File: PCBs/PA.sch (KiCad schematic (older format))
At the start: 16 parts, among them K1 TIANBO-HJR-4102-L, Q4 BS170, Q6 BS170, Q8 BS170, Q9 BC849, U1 74AC14

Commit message: ADX988 CAT: add FE, FI commands
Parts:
- C27: footprint Capacitors_THT:C_Disc_D4.7mm_W2.5mm_P5.00mm -> LCSDR:C_1206_0603
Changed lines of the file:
@@
 $Descr A4 11693 8268
 encoding utf-8
-Sheet 6 9
+Sheet 6 8
 Title ""
 Date ""
@@
 Connection ~ 6150 2800
 $Comp
-L GND #PWR060
+L GND #PWR83
 U 1 1 63065D00
 P 6700 3050
-F 0 "#PWR060" H 6700 2800 50  0001 C CNN
+F 0 "#PWR83" H 6700 2800 50  0001 C CNN
 F 1 "GND" H 6700 2900 50  0001 C CNN
 F 2 "" H 6700 3050 50  0001 C CNN
@@
 	6700 3050 6700 3000
 $Comp
-L GND #PWR061
+L GND #PWR85
 U 1 1 63065D9F
 P 7350 3750
-F 0 "#PWR061" H 7350 3500 50  0001 C CNN
+F 0 "#PWR85" H 7350 3500 50  0001 C CNN
 F 1 "GND" H 7350 3600 50  0001 C CNN
 F 2 "" H 7350 3750 50  0001 C CNN
@@
 	7350 3750 7350 3700
 $Comp
-L GND #PWR062
+L GND #PWR81
 U 1 1 63065E88
 P 4850 2600
-F 0 "#PWR062" H 4850 2350 50  0001 C CNN
+F 0 "#PWR81" H 4850 2350 50  0001 C CNN
 F 1 "GND" H 4850 2450 50  0001 C CNN
 F 2 "" H 4850 2600 50  0001 C CNN
@@
 Connection ~ 2100 5500
 $Comp
-L GND #PWR063
+L GND #PWR75
 U 1 1 630683A0
 P 2850 5700
-F 0 "#PWR063" H 2850 5450 50  0001 C CNN
+F 0 "#PWR75" H 2850 5450 50  0001 C CNN
 F 1 "GND" H 2850 5550 50  0001 C CNN
 F 2 "" H 2850 5700 50  0001 C CNN
@@
 $EndComp
 $Comp
-L +5V #PWR064
+L +5V #PWR74
 U 1 1 6306844B
 P 2850 5300
-F 0 "#PWR064" H 2850 5150 50  0001 C CNN
+F 0 "#PWR74" H 2850 5150 50  0001 C CNN
 F 1 "+5V" H 2850 5440 50  0000 C CNN
 F 2 "" H 2850 5300 50  0001 C CNN
@@
 $EndComp
 $Comp
-L GND #PWR065
+L GND #PWR73
 U 1 1 6306851D
 P 2850 4550
-F 0 "#PWR065" H 2850 4300 50  0001 C CNN
+F 0 "#PWR73" H 2850 4300 50  0001 C CNN
 F 1 "GND" H 2850 4400 50  0001 C CNN
 F 2 "" H 2850 4550 50  0001 C CNN
@@
 	2850 4550 2850 4450
 $Comp
-L +5V #PWR066
+L +5V #PWR72
 U 1 1 63068670
 P 2850 4150
-F 0 "#PWR066" H 2850 4000 50  0001 C CNN
+F 0 "#PWR72" H 2850 4000 50  0001 C CNN
 F 1 "+5V" H 2850 4290 50  0000 C CNN
 F 2 "" H 2850 4150 50  0001 C CNN
@@
 	2850 4150 2850 4250
 $Comp
-L GND #PWR067
+L GND #PWR80
 U 1 1 63068793
 P 4350 2600
-F 0 "#PWR067" H 4350 2350 50  0001 C CNN
+F 0 "#PWR80" H 4350 2350 50  0001 C CNN
 F 1 "GND" H 4350 2450 50  0001 C CNN
 F 2 "" H 4350 2600 50  0001 C CNN
@@
 CLK0
 $Comp
-L GND #PWR068
+L GND #PWR77
 U 1 1 63068BDA
 P 2850 6850
-F 0 "#PWR068" H 2850 6600 50  0001 C CNN
+F 0 "#PWR77" H 2850 6600 50  0001 C CNN
 F 1 "GND" H 2850 6700 50  0001 C CNN
 F 2 "" H 2850 6850 50  0001 C CNN
@@
 	2850 6850 2850 6750
 $Comp
-L +5V #PWR069
+L +5V #PWR76
 U 1 1 63068C63
 P 2850 6450
-F 0 "#PWR069" H 2850 6300 50  0001 C CNN
+F 0 "#PWR76" H 2850 6300 50  0001 C CNN
 F 1 "+5V" H 2850 6590 50  0000 C CNN
 F 2 "" H 2850 6450 50  0001 C CNN
@@
 	2850 6450 2850 6550
 $Comp
-L GND #PWR070
+L GND #PWR71
 U 1 1 63068D65
 P 2850 3500
-F 0 "#PWR070" H 2850 3250 50  0001 C CNN
+F 0 "#PWR71" H 2850 3250 50  0001 C CNN
 F 1 "GND" H 2850 3350 50  0001 C CNN
 F 2 "" H 2850 3500 50  0001 C CNN
@@
 	2850 3200 2850 3100
 $Comp
-L +5V #PWR071
+L +5V #PWR70
 U 1 1 63068E93
 P 2850 3100
-F 0 "#PWR071" H 2850 2950 50  0001 C CNN
+F 0 "#PWR70" H 2850 2950 50  0001 C CNN
 F 1 "+5V" H 2850 3240 50  0000 C CNN
 F 2 "" H 2850 3100 50  0001 C CNN
@@
 $EndComp
 $Comp
-L GND #PWR072
+L GND #PWR69
 U 1 1 63068F01
 P 2850 2500
-F 0 "#PWR072" H 2850 2250 50  0001 C CNN
+F 0 "#PWR69" H 2850 2250 50  0001 C CNN
 F 1 "GND" H 2850 2350 50  0001 C CNN
 F 2 "" H 2850 2500 50  0001 C CNN
@@
 	2850 2500 2850 2400
 $Comp
-L +5V #PWR073
+L +5V #PWR68
 U 1 1 63069009
 P 2850 2100
-F 0 "#PWR073" H 2850 1950 50  0001 C CNN
+F 0 "#PWR68" H 2850 1950 50  0001 C CNN
 F 1 "+5V" H 2850 2240 50  0000 C CNN
 F 2 "" H 2850 2100 50  0001 C CNN
@@
 	2850 2100 2850 2200
 $Comp
-L +5V #PWR074
+L +5V #PWR66
 U 1 1 63069127
 P 2850 1000
-F 0 "#PWR074" H 2850 850 50  0001 C CNN
+F 0 "#PWR66" H 2850 850 50  0001 C CNN
 F 1 "+5V" H 2850 1140 50  0000 C CNN
 F 2 "" H 2850 1000 50  0001 C CNN
@@
 $EndComp
 $Comp
-L GND #PWR075
+L GND #PWR67
 U 1 1 6306916E
 P 2850 1400
-F 0 "#PWR075" H 2850 1150 50  0001 C CNN
+F 0 "#PWR67" H 2850 1150 50  0001 C CNN
 F 1 "GND" H 2850 1250 50  0001 C CNN
 F 2 "" H 2850 1400 50  0001 C CNN
@@
 $EndComp
 $Comp
-L GND #PWR076
+L GND #PWR79
 U 1 1 6306940A
 P 4150 1400
-F 0 "#PWR076" H 4150 1150 50  0001 C CNN
+F 0 "#PWR79" H 4150 1150 50  0001 C CNN
 F 1 "GND" H 4150 1250 50  0001 C CNN
 F 2 "" H 4150 1400 50  0001 C CNN
@@
 	4150 1350 4150 1400
 $Comp
-L +5V #PWR077
+L +5V #PWR78
 U 1 1 630694A1
 P 4150 1100
-F 0 "#PWR077" H 4150 950 50  0001 C CNN
+F 0 "#PWR78" H 4150 950 50  0001 C CNN
 F 1 "+5V" H 4150 1240 50  0000 C CNN
 F 2 "" H 4150 1100 50  0001 C CNN
@@
 F 0 "C27" H 8100 3600 50  0000 L CNN
 F 1 "100pF" H 8100 3500 50  0000 L CNN
-F 2 "Capacitors_THT:C_Disc_D4.7mm_W2.5mm_P5.00mm" H 8000 3500 50  0001 C CNN
+F 2 "LCSDR:C_1206_0603" H 8000 3500 50  0001 C CNN
 F 3 "" H 8000 3500 50  0001 C CNN
 	1    8000 3500
@@
 $EndComp
 $Comp
-L GND #PWR078
+L GND #PWR86
 U 1 1 6306993E
 P 8000 3700
-F 0 "#PWR078" H 8000 3450 50  0001 C CNN
+F 0 "#PWR86" H 8000 3450 50  0001 C CNN
 F 1 "GND" H 8000 3550 50  0001 C CNN
 F 2 "" H 8000 3700 50  0001 C CNN
@@
 $EndComp
 $Comp
-L GND #PWR079
+L GND #PWR89
 U 1 1 6306C621
 P 9750 5200
-F 0 "#PWR079" H 9750 4950 50  0001 C CNN
+F 0 "#PWR89" H 9750 4950 50  0001 C CNN
 F 1 "GND" H 9750 5050 50  0001 C CNN
 F 2 "" H 9750 5200 50  0001 C CNN
@@
 $EndComp
 $Comp
-L +12V #PWR080
+L +12V #PWR87
 U 1 1 6306CB0A
 P 8900 3600
-F 0 "#PWR080" H 8900 3450 50  0001 C CNN
+F 0 "#PWR87" H 8900 3450 50  0001 C CNN
 F 1 "+12V" V 8900 3800 50  0000 C CNN
 F 2 "" H 8900 3600 50  0001 C CNN
@@
 $EndComp
 $Comp
-L GND #PWR081
+L GND #PWR88
 U 1 1 630A2E88
 P 9050 5300
-F 0 "#PWR081" H 9050 5050 50  0001 C CNN
+F 0 "#PWR88" H 9050 5050 50  0001 C CNN
 F 1 "GND" H 9050 5150 50  0001 C CNN
 F 2 "" H 9050 5300 50  0001 C CNN
@@
 RX_TX
 $Comp
-L +12VA #PWR082
+L +12VA #PWR84
 U 1 1 630BAC82
 P 7350 1850
-F 0 "#PWR082" H 7350 1700 50  0001 C CNN
+F 0 "#PWR84" H 7350 1700 50  0001 C CNN
 F 1 "+12VA" H 7350 1990 50  0000 C CNN
 F 2 "" H 7350 1850 50  0001 C CNN
@@
 Connection ~ 6700 2400
 $Comp
-L GND #PWR083
+L GND #PWR82
 U 1 1 630BE9B9
 P 6150 2500
-F 0 "#PWR083" H 6150 2250 50  0001 C CNN
+F 0 "#PWR82" H 6150 2250 50  0001 C CNN
 F 1 "GND" H 6150 2350 50  0001 C CNN
 F 2 "" H 6150 2500 50  0001 C CNN

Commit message: discret, simple, CH340E
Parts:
- removed C25: 100nF, LCSDR:C_1206_0603, symbol C_Small
- removed D1: LL4148, Diodes_SMD:D_MiniMELF, symbol D_Small
- removed U1: 74AC14, Housings_DIP:DIP-14_W7.62mm_LongPads, symbol 74HC14
- added R27, R28: 1R, LCSDR:R_1206_0603, symbol R_Small
- added U7: 74ACT00, Housings_SOIC:SOIC-14_3.9x8.7mm_Pitch1.27mm, symbol 74HC00
- C26: footprint LCSDR:C_1206_0603 -> Capacitors_SMD:C_0603_HandSoldering
- R14: value 2.7K -> 1R
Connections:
- wire segments 69 -> 57
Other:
- moved on the sheet: Q4, Q6, Q8

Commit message: INIT project, si5351 generate properly frequency
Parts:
- C27: value 100pF -> 100nF; footprint LCSDR:C_1206_0603 -> Capacitors_SMD:C_0603_HandSoldering
- C28: value 100pF -> 15nF; footprint LCSDR:C_1206_0603 -> Capacitors_SMD:C_0603_HandSoldering
- C29: footprint LCSDR:C_1206_0603 -> Capacitors_SMD:C_0603_HandSoldering
- R15: footprint LCSDR:R_1206_0603 -> Resistors_SMD:R_0603_HandSoldering
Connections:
- net RX_TX: no longer U7.2
- new net RX_TX_PA: U7.2
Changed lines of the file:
@@
 $Descr A4 11693 8268
 encoding utf-8
-Sheet 6 8
+Sheet 6 7
 Title ""
 Date ""
@@
 $EndComp
 $Comp
-L GND #PWR065
+L GND #PWR061
 U 1 1 63065D00
 P 6700 3800
-F 0 "#PWR065" H 6700 3550 50  0001 C CNN
+F 0 "#PWR061" H 6700 3550 50  0001 C CNN
 F 1 "GND" H 6700 3650 50  0001 C CNN
 F 2 "" H 6700 3800 50  0001 C CNN
@@
 	6700 3550 6700 3500
 $Comp
-L GND #PWR066
+L GND #PWR062
 U 1 1 63065D9F
 P 7350 4450
-F 0 "#PWR066" H 7350 4200 50  0001 C CNN
+F 0 "#PWR062" H 7350 4200 50  0001 C CNN
 F 1 "GND" H 7350 4300 50  0001 C CNN
 F 2 "" H 7350 4450 50  0001 C CNN
@@
 $EndComp
 $Comp
-L GND #PWR067
+L GND #PWR063
 U 1 1 6306940A
 P 4150 1400
-F 0 "#PWR067" H 4150 1150 50  0001 C CNN
+F 0 "#PWR063" H 4150 1150 50  0001 C CNN
 F 1 "GND" H 4150 1250 50  0001 C CNN
 F 2 "" H 4150 1400 50  0001 C CNN
@@
 	4150 1350 4150 1400
 $Comp
-L +5V #PWR068
+L +5V #PWR064
 U 1 1 630694A1
 P 4150 1100
-F 0 "#PWR068" H 4150 950 50  0001 C CNN
+F 0 "#PWR064" H 4150 950 50  0001 C CNN
 F 1 "+5V" H 4150 1240 50  0000 C CNN
 F 2 "" H 4150 1100 50  0001 C CNN
@@
 P 8000 3500
 F 0 "C27" H 8100 3600 50  0000 L CNN
-F 1 "100pF" H 8100 3500 50  0000 L CNN
-F 2 "LCSDR:C_1206_0603" H 8000 3500 50  0001 C CNN
+F 1 "100nF" H 8100 3500 50  0000 L CNN
+F 2 "Capacitors_SMD:C_0603_HandSoldering" H 8000 3500 50  0001 C CNN
 F 3 "" H 8000 3500 50  0001 C CNN
 	1    8000 3500
@@
 $EndComp
 $Comp
-L GND #PWR069
+L GND #PWR065
 U 1 1 6306993E
 P 8000 3700
-F 0 "#PWR069" H 8000 3450 50  0001 C CNN
+F 0 "#PWR065" H 8000 3450 50  0001 C CNN
 F 1 "GND" H 8000 3550 50  0001 C CNN
 F 2 "" H 8000 3700 50  0001 C CNN
@@
 F 0 "C29" V 8500 3050 50  0000 L CNN
 F 1 "100nF" V 8400 2900 50  0000 L CNN
-F 2 "LCSDR:C_1206_0603" H 8250 3100 50  0001 C CNN
+F 2 "Capacitors_SMD:C_0603_HandSoldering" H 8250 3100 50  0001 C CNN
 F 3 "" H 8250 3100 50  0001 C CNN
 	1    8250 3100
@@
 $EndComp
 $Comp
-L GND #PWR070
+L GND #PWR066
 U 1 1 6306C621
 P 9750 5200
-F 0 "#PWR070" H 9750 4950 50  0001 C CNN
+F 0 "#PWR066" H 9750 4950 50  0001 C CNN
 F 1 "GND" H 9750 5050 50  0001 C CNN
 F 2 "" H 9750 5200 50  0001 C CNN
@@
 $EndComp
 $Comp
-L +12V #PWR071
+L +12V #PWR067
 U 1 1 6306CB0A
 P 8900 3600
-F 0 "#PWR071" H 8900 3450 50  0001 C CNN
+F 0 "#PWR067" H 8900 3450 50  0001 C CNN
 F 1 "+12V" V 8900 3800 50  0000 C CNN
 F 2 "" H 8900 3600 50  0001 C CNN
@@
 F 0 "R15" V 8500 4900 50  0000 L CNN
 F 1 "3.3k" V 8600 4900 50  0000 L CNN
-F 2 "LCSDR:R_1206_0603" H 8700 4950 50  0001 C CNN
+F 2 "Resistors_SMD:R_0603_HandSoldering" H 8700 4950 50  0001 C CNN
 F 3 "" H 8700 4950 50  0001 C CNN
 	1    8700 4950
@@
 P 9050 5150
 F 0 "C28" H 9150 5250 50  0000 L CNN
-F 1 "100pF" H 9150 5150 50  0000 L CNN
-F 2 "LCSDR:C_1206_0603" H 9050 5150 50  0001 C CNN
+F 1 "15nF" H 9150 5150 50  0000 L CNN
+F 2 "Capacitors_SMD:C_0603_HandSoldering" H 9050 5150 50  0001 C CNN
 F 3 "" H 9050 5150 50  0001 C CNN
 	1    9050 5150
@@
 $EndComp
 $Comp
-L GND #PWR072
+L GND #PWR068
 U 1 1 630A2E88
 P 9050 5300
-F 0 "#PWR072" H 9050 5050 50  0001 C CNN
+F 0 "#PWR068" H 9050 5050 50  0001 C CNN
 F 1 "GND" H 9050 5150 50  0001 C CNN
 F 2 "" H 9050 5300 50  0001 C CNN
@@
 RX_TX
 $Comp
-L +12VA #PWR073
+L +12VA #PWR069
 U 1 1 630BAC82
 P 7350 2050
-F 0 "#PWR073" H 7350 1900 50  0001 C CNN
+F 0 "#PWR069" H 7350 1900 50  0001 C CNN
 F 1 "+12VA" H 7350 2190 50  0000 C CNN
 F 2 "" H 7350 2050 50  0001 C CNN
@@
 $EndComp
 $Comp
-L GND #PWR074
+L GND #PWR070
 U 1 1 630BE9B9
 P 6150 3150
-F 0 "#PWR074" H 6150 2900 50  0001 C CNN
+F 0 "#PWR070" H 6150 2900 50  0001 C CNN
 F 1 "GND" H 6150 3000 50  0001 C CNN
 F 2 "" H 6150 3150 50  0001 C CNN
@@
 Connection ~ 8950 3600
 $Comp
-L GND #PWR075
+L GND #PWR071
 U 1 1 63068F01
 P 4350 2900
-F 0 "#PWR075" H 4350 2650 50  0001 C CNN
+F 0 "#PWR071" H 4350 2650 50  0001 C CNN
 F 1 "GND" H 4350 2750 50  0001 C CNN
 F 2 "" H 4350 2900 50  0001 C CNN
@@
 	4350 2450 4350 2400
 $Comp
-L +5V #PWR076
+L +5V #PWR072
 U 1 1 63825BAA
 P 4350 2400
-F 0 "#PWR076" H 4350 2250 50  0001 C CNN
+F 0 "#PWR072" H 4350 2250 50  0001 C CNN
 F 1 "+5V" H 4350 2540 50  0000 C CNN
 F 2 "" H 4350 2400 50  0001 C CNN
@@
 	4350 3350 4350 3300
 $Comp
-L +5V #PWR077
+L +5V #PWR073
 U 1 1 63827BD8
 P 4350 3300
-F 0 "#PWR077" H 4350 3150 50  0001 C CNN
+F 0 "#PWR073" H 4350 3150 50  0001 C CNN
 F 1 "+5V" H 4350 3440 50  0000 C CNN
 F 2 "" H 4350 3300 50  0001 C CNN
@@
 	2550 2450 2200 2450
 Text GLabel 2500 2650 0    60   Input ~ 0
-RX_TX
+RX_TX_PA
 Wire Wire Line
 	2500 2650 2550 2650
@@
 $EndComp
 $Comp
-L +5V #PWR078
+L +5V #PWR074
 U 1 1 6382FF4D
 P 4350 4150
-F 0 "#PWR078" H 4350 4000 50  0001 C CNN
+F 0 "#PWR074" H 4350 4000 50  0001 C CNN
 F 1 "+5V" H 4350 4290 50  0000 C CNN
 F 2 "" H 4350 4150 50  0001 C CNN
@@
 	4350 4150 4350 4200
 $Comp
-L GND #PWR079
+L GND #PWR075
 U 1 1 63830324
 P 4350 3800
-F 0 "#PWR079" H 4350 3550 50  0001 C CNN
+F 0 "#PWR075" H 4350 3550 50  0001 C CNN
 F 1 "GND" H 4350 3650 50  0001 C CNN
 F 2 "" H 4350 3800 50  0001 C CNN
@@
 	2950 2750 2950 2800
 $Comp
-L GND #PWR080
+L GND #PWR076
 U 1 1 638313B1
 P 4350 4650
-F 0 "#PWR080" H 4350 4400 50  0001 C CNN
+F 0 "#PWR076" H 4350 4400 50  0001 C CNN
 F 1 "GND" H 4350 4500 50  0001 C CNN
 F 2 "" H 4350 4650 50  0001 C CNN
@@
 	4350 4650 4350 4600
 $Comp
-L GND #PWR081
+L GND #PWR077
 U 1 1 638314CD
 P 2950 2800
-F 0 "#PWR081" H 2950 2550 50  0001 C CNN
+F 0 "#PWR077" H 2950 2550 50  0001 C CNN
 F 1 "GND" H 2950 2650 50  0001 C CNN
 F 2 "" H 2950 2800 50  0001 C CNN
@@
 $EndComp
 $Comp
-L +5V #PWR082
+L +5V #PWR078
 U 1 1 6383152C
 P 2950 2300
-F 0 "#PWR082" H 2950 2150 50  0001 C CNN
+F 0 "#PWR078" H 2950 2150 50  0001 C CNN
 F 1 "+5V" H 2950 2440 50  0000 C CNN
 F 2 "" H 2950 2300 50  0001 C CNN

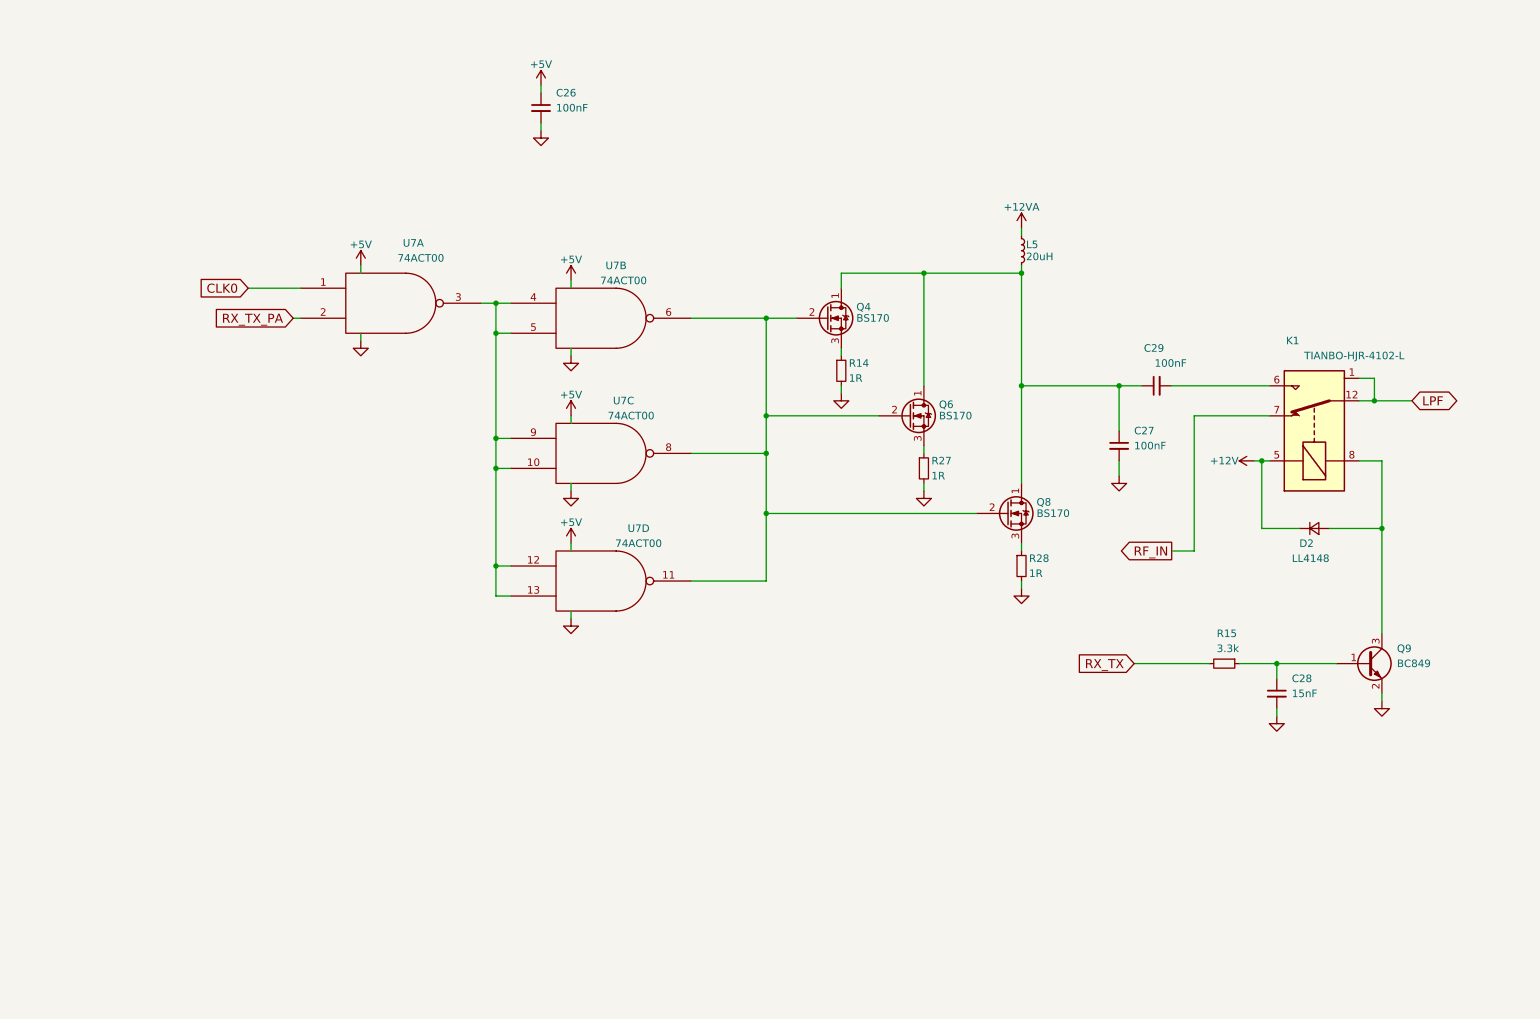
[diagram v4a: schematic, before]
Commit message: migrate to attiny1614
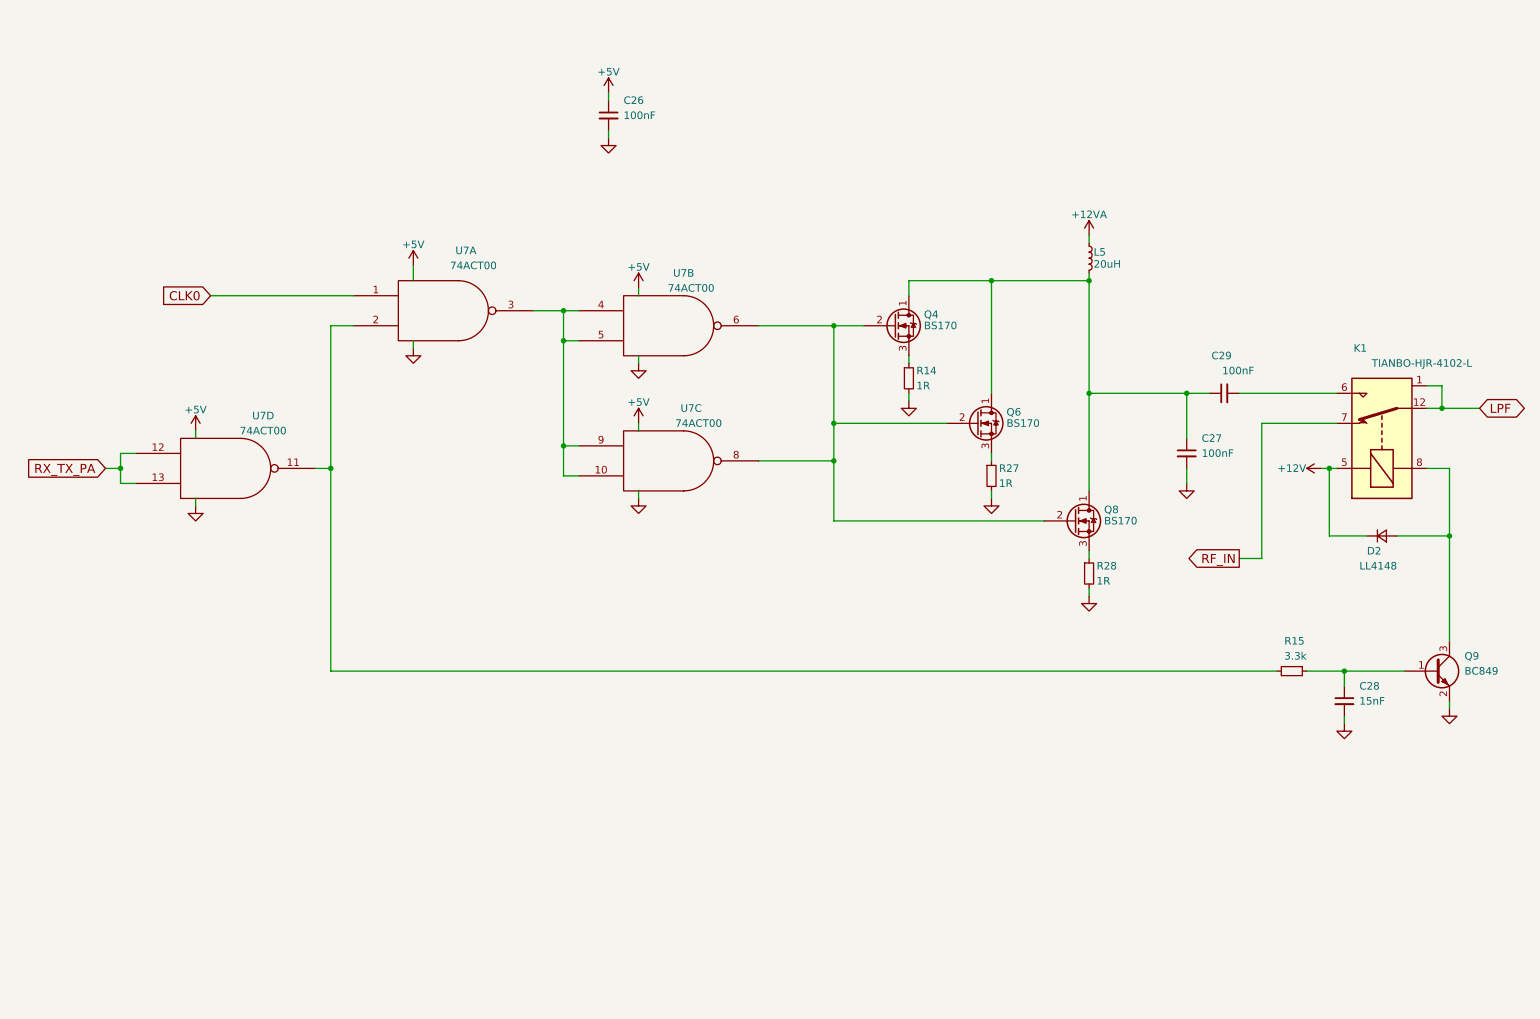
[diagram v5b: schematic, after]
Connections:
- net RX_TX_PA: now also U7.12, U7.13; no longer U7.2
- net at Q4.2 (G), Q6.2 (G), Q8.2 (G)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: no longer U7.11
- net at U7.10, U7.3, U7.4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: no longer U7.12, U7.13
- net RX_TX: no longer names the net of R15.2
- net RX_TX: now also U7.11, U7.2
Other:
- moved on the sheet: C26, C27, C28, C29, D2, K1, L5, Q4, Q6, Q8, Q9, R14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
